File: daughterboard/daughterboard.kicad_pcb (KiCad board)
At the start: 2 copper layers, 49 x 51 mm, 19 parts, among them J1 Conn_02x07_Odd_Even, J2 Conn_01x01, J3 Conn_01x01, J4 Conn_01x01, J5 Conn_01x01, SW1 SW_Push, SW2 Rotary_Encoder_Switch_Alps, SW3 SW_Push, SW4 SW_Push

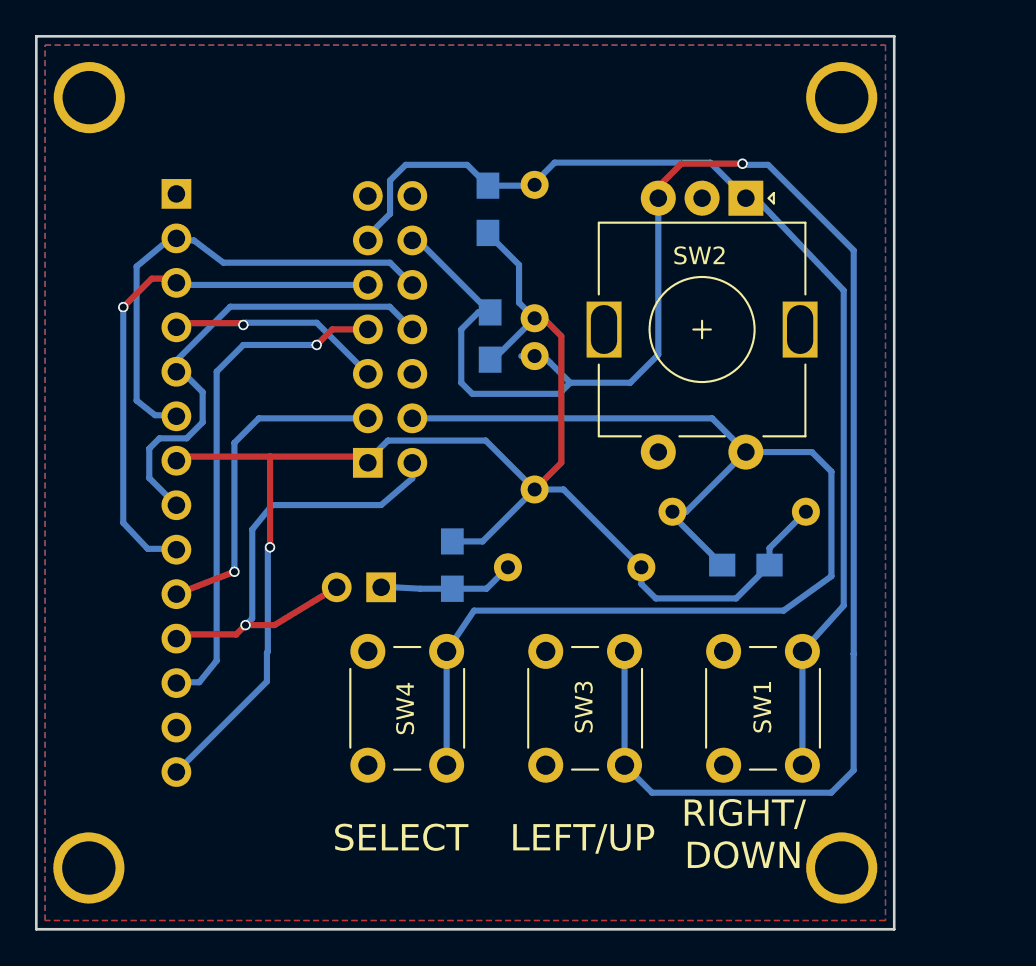
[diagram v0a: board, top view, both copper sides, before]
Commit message: Moved mounting holes to ensure no interference
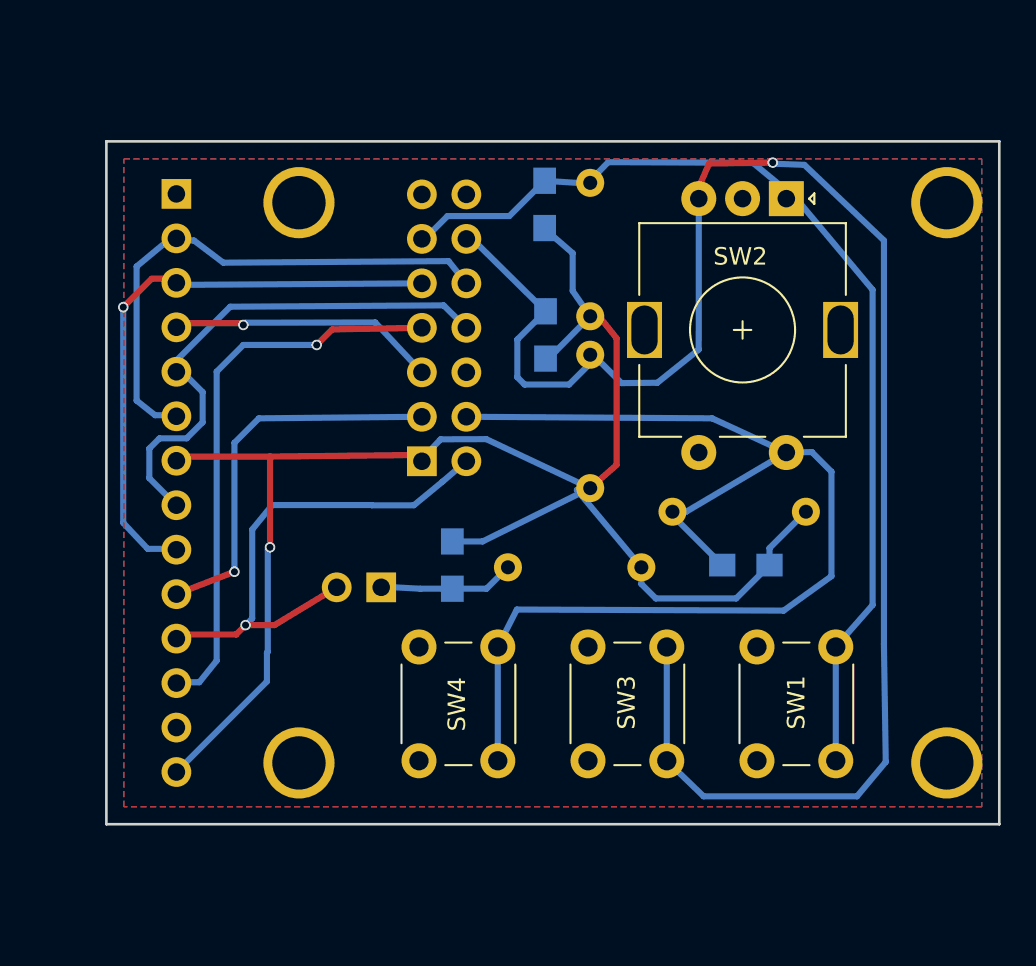
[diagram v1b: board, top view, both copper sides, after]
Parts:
- moved J4 13.4 mm to (111.0, 87.5), turned to 270 degrees
- moved J2 13.4 mm to (111.0, 55.5)
- moved J3 8.49 mm to (148.0, 87.5)
- moved J5 8.49 mm to (148.0, 55.5)
- moved R3 3.25 mm to (125.0, 55.6)
- moved R4 3.18 mm to (127.6, 62.0)
- moved R2 3.18 mm to (127.6, 71.8)
- moved R1 3.16 mm to (125.1, 63.1)
- moved J1 3.09 mm to (118.0, 70.3)
- moved SW4 2.93 mm to (117.9, 87.4)
- moved SW3 2.43 mm to (127.5, 87.4)
- moved SW2 2.31 mm to (138.8, 55.3)
- moved SW1 1.92 mm to (137.2, 87.4)
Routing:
- net CS5: track 71.4 -> 66.9 mm
- net +5V: track 91.9 -> 96.1 mm
- net MISO: track 27.4 -> 30.6 mm
- net CS2: track 12.8 -> 16.0 mm
- net CS1: track 29.4 -> 32.5 mm
- net CS3: track 19.8 -> 22.8 mm
- net MOSI: track 30.5 -> 33.5 mm
- net SCK: track 27.4 -> 30.5 mm
- net INTF2: track 102.0 -> 98.9 mm
- net CS4: track 27.3 -> 29.8 mm
- net INTF1: track 62.5 -> 60.6 mm
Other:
- board size 49 x 51 mm -> 51 x 39 mm
- board text added: "VNA LCD INTERFACE KW4TI CC-BY-SA 4.0"
- board text removed: "LEFT/UP"
- board text removed: "RIGHT/ DOWN"
- board text removed: "SELECT"
- board text removed: "VNA LCD INTERFACE BOARD ILI9341/ILI9488 SPI LCD TOUCHSCREEN BY KW4TI CC-BY-SA 4.0"

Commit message: Added debouncing capacitors
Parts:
- added C1: C_Small, Capacitors_SMD:C_0805_HandSoldering, B.Cu at (145.5, 69.0)
- added C2: C_Small, Capacitors_THT:C_Disc_D5.0mm_W2.5mm_P2.50mm, B.Cu at (145.5, 61.9)
- added C3: C_Small, Capacitors_SMD:C_0805_HandSoldering, B.Cu at (145.5, 73.9)
- added C4: C_Small, Capacitors_THT:C_Disc_D5.0mm_W2.5mm_P2.50mm, B.Cu at (148.1, 64.8)
- added C5: C_Small, Capacitors_SMD:C_0805_HandSoldering, B.Cu at (113.9, 81.3)
- added C6: C_Small, Capacitors_THT:C_Disc_D5.0mm_W2.5mm_P2.50mm, B.Cu at (115.6, 78.4)
- moved JP1 2.29 mm to (115.6, 75.2)
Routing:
- net CS5: track 66.9 -> 77.8 mm
- net INTF2: track 98.9 -> 109.2 mm
- net GND: track 0.00 -> 3.32 mm, vias 0 -> 2
- net INTF1: track 60.6 -> 62.5 mm
- net CS4: track 29.8 -> 31.6 mm
- net Net-(JP1-Pad1): track 7.75 -> 8.65 mm

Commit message: Added resistors in discharge debounce
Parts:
- added R10: 100R, Resistors_THT:R_Axial_DIN0207_L6.3mm_D2.5mm_P7.62mm_Horizontal, B.Cu at (145.7, 61.9)
- added R11: 100R, Resistors_SMD:R_0805_HandSoldering, B.Cu at (146.8, 82.5)
- added R12: 100R, Resistors_THT:R_Axial_DIN0207_L6.3mm_D2.5mm_P7.62mm_Horizontal, B.Cu at (148.2, 80.5)
- added R13: 100R, Resistors_SMD:R_0805_HandSoldering, B.Cu at (110.9, 80.3)
- added R14: 100R, Resistors_THT:R_Axial_DIN0207_L6.3mm_D2.5mm_P7.62mm_Horizontal, B.Cu at (115.1, 74.5)
- added R9: 100R, Resistors_SMD:R_0805_HandSoldering, B.Cu at (146.7, 59.7)
- C1, C2, C3, C4, C5, C6: value C_Small -> 100 nF
- R1, R2, R3, R4, R5, R6, R7, R8: value 10k -> 100k
- moved C4 15.1 mm to (145.0, 79.6), turned to 90 degrees
- moved C6 5.76 mm to (111.9, 82.8)
- moved C5 5.08 mm to (115.4, 86.1), turned to 270 degrees
- moved JP1 4.36 mm to (111.6, 77.1), turned to 0 degrees
- moved C1 3.15 mm to (148.7, 69.2), turned to 90 degrees
- moved C2 2.86 mm to (148.4, 62.4), turned to 270 degrees
- moved C3 0.89 mm to (145.4, 73.0), turned to 270 degrees
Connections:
- C1 pad 1: INTF1 -> Net-(C1-Pad1)
- C2 pad 1: INTF1 -> Net-(C1-Pad1)
- C3 pad 1: INTF2 -> Net-(C3-Pad1)
- C4 pad 1: INTF2 -> Net-(C3-Pad1)
- C5 pad 1: CS5 -> Net-(C5-Pad1)
- C6 pad 1: CS5 -> Net-(C5-Pad1)
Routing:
- net Net-(C1-Pad1): track 0.00 -> 15.7 mm
- net Net-(C3-Pad1): track 0.00 -> 15.3 mm
- net Net-(JP1-Pad1): track 8.65 -> 18.4 mm
- net Net-(C5-Pad1): track 0.00 -> 9.42 mm
- net CS5: track 77.8 -> 85.4 mm
- net INTF2: track 109.2 -> 116.6 mm
- net CS4: track 31.6 -> 27.5 mm
- net GND: track 3.32 -> 6.33 mm, vias 2 -> 0
- net +5V: track 96.1 -> 99.0 mm
- net INTF1: track 62.5 -> 64.4 mm
- net CS3: track 22.8 -> 21.9 mm

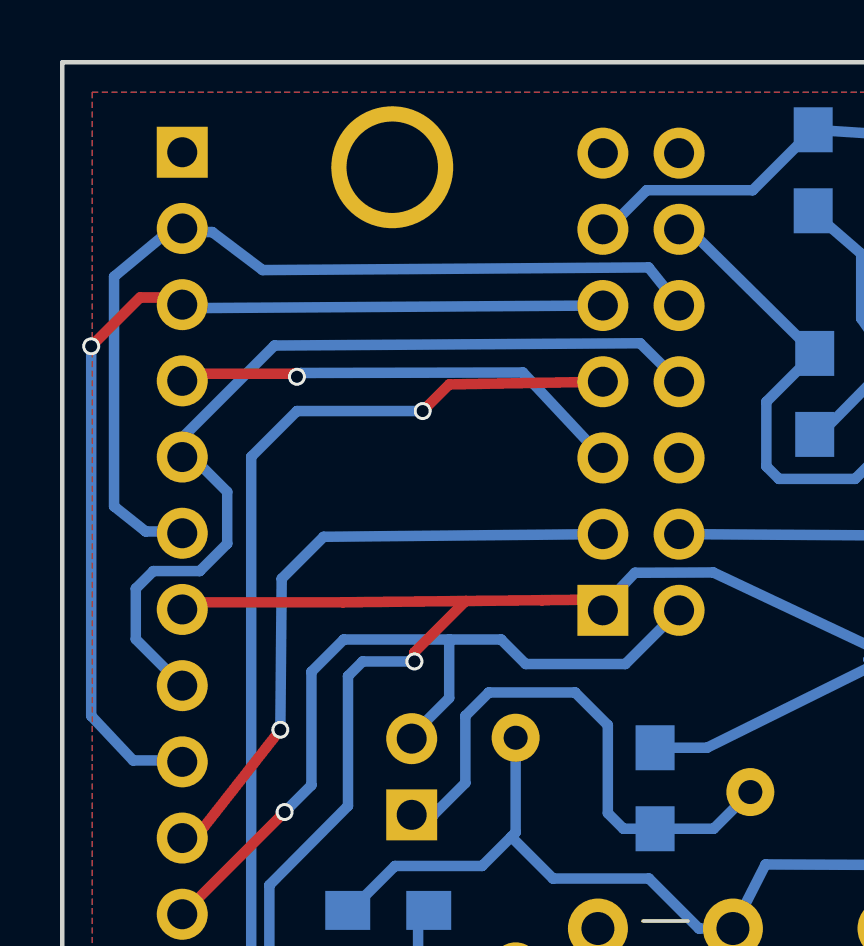
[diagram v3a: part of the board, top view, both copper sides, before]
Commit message: Added vacuum holes to fixture
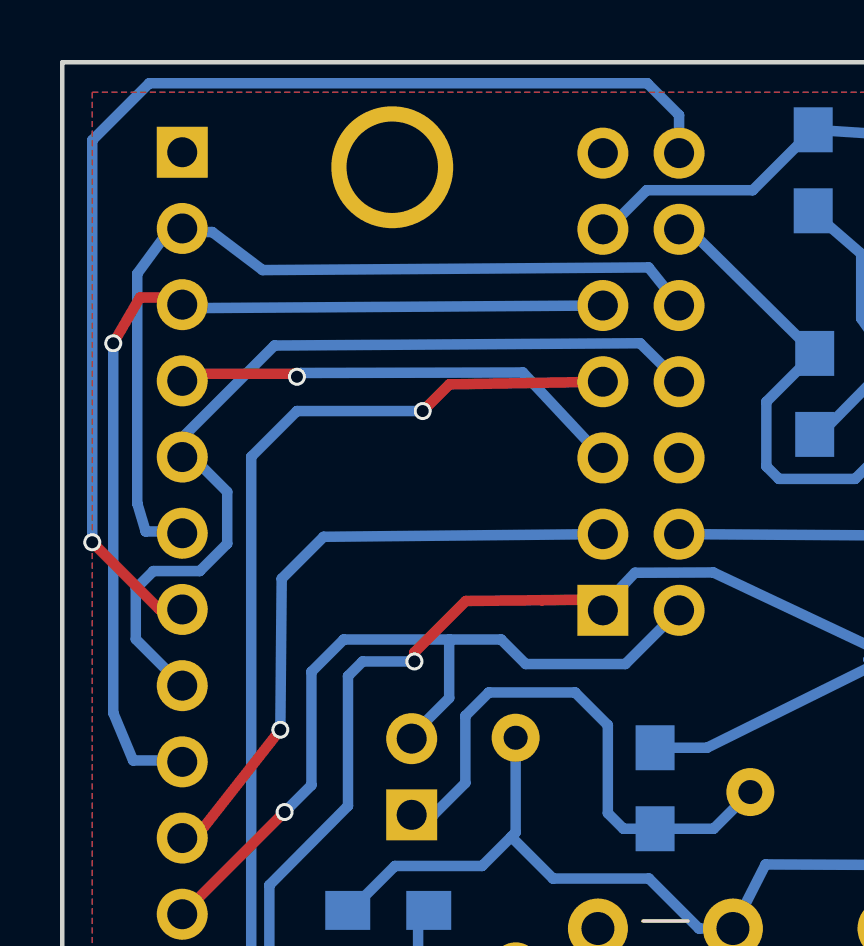
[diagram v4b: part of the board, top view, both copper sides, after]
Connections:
- DISP1 pad 7: +5V -> LEDPWR
- J1 pad 14: (no net) -> LEDPWR
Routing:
- net LEDPWR: track 0.00 -> 39.9 mm, vias 0 -> 1
- net +5V: track 99.0 -> 88.7 mm
- net MISO: track 30.6 -> 29.6 mm
- net MOSI: track 33.5 -> 32.7 mm
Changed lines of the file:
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@@
     (links 68)
     (no_connects 0)
-    (area 99.924999 51.924999 151.075001 91.075001)
+    (area 99.924999 51.525 164.1584 92.247619)
     (thickness 1.6)
     (drawings 6)
-    (tracks 246)
+    (tracks 252)
     (zones 0)
     (modules 31)
-    (nets 17)
+    (nets 18)
   )
   (page A4)
@@
   (net 15 "Net-(C3-Pad1)")
   (net 16 "Net-(C5-Pad1)")
+  (net 17 LEDPWR)
   (net_class Default "This is the default net class."
     (clearance 0.2)
@@
     (add_net INTF1)
     (add_net INTF2)
+    (add_net LEDPWR)
     (add_net MISO)
     (add_net MOSI)
@@
       (net 12 INTF2))
     (pad 13 thru_hole oval (at 0 -15.24) (size 1.7 1.7) (drill 1) (layers *.Cu *.Mask))
-    (pad 14 thru_hole oval (at 2.54 -15.24) (size 1.7 1.7) (drill 1) (layers *.Cu *.Mask))
+    (pad 14 thru_hole oval (at 2.54 -15.24) (size 1.7 1.7) (drill 1) (layers *.Cu *.Mask)
+      (net 17 LEDPWR))
     (model ${KISYS3DMOD}/Pin_Headers.3dshapes/Pin_Header_Straight_2x07_Pitch2.54mm.wrl
       (at (xyz 0 0 0))
@@
       (net 10 MISO))
     (pad 7 thru_hole oval (at 0 -15.24 180) (size 1.7 1.7) (drill 1) (layers *.Cu *.Mask)
-      (net 1 +5V))
+      (net 17 LEDPWR))
     (pad 8 thru_hole oval (at 0 -17.78 180) (size 1.7 1.7) (drill 1) (layers *.Cu *.Mask)
       (net 8 SCK))
@@
     (effects (font (size 1.5 1.5) (thickness 0.3)) (justify mirror))
   )
-  (segment (start 111.73968 71.97344) (end 111.73968 71.66864) (width 0.35) (layer F.Cu) (net 1))
-  (segment (start 111.73968 71.66864) (end 113.449766 69.958554) (width 0.35) (layer F.Cu) (net 1))
   (segment (start 104.3088 88.02) (end 106.90352 85.4456) (width 0.35) (layer B.Cu) (net 1))
   (segment (start 115.976455 69.931225) (end 116.006946 69.931225) (width 0.35) (layer F.Cu) (net 1))
-  (via (at 111.73968 71.97344) (size 0.6) (drill 0.4) (layers F.Cu B.Cu) (net 1))
-  (segment (start 110.01248 71.97344) (end 111.73968 71.97344) (width 0.35) (layer B.Cu) (net 1))
-  (segment (start 109.5248 72.46112) (end 110.01248 71.97344) (width 0.35) (layer B.Cu) (net 1))
   (segment (start 109.5248 76.78928) (end 109.5248 72.46112) (width 0.35) (layer B.Cu) (net 1))
   (segment (start 106.90352 79.43088) (end 109.5248 76.78928) (width 0.35) (layer B.Cu) (net 1))
@@
   (segment (start 119.761 74.85) (end 121.492 74.85) (width 0.35) (layer B.Cu) (net 1))
   (segment (start 121.492 74.85) (end 127.635 71.8058) (width 0.35) (layer B.Cu) (net 1) (status 20))
-  (segment (start 103.57104 70.0024) (end 109.347 70.0024) (width 0.35) (layer F.Cu) (net 1))
-  (segment (start 109.347 70.0024) (end 113.449766 69.958554) (width 0.35) (layer F.Cu) (net 1) (status 20))
   (segment (start 113.449766 69.958554) (end 116.006946 69.931225) (width 0.35) (layer F.Cu) (net 1) (status 20))
   (segment (start 116.006946 69.931225) (end 117.6655 69.9135) (width 0.35) (layer F.Cu) (net 1) (status 20))
   (segment (start 117.6655 69.9135) (end 118.0211 70.2691) (width 0.35) (layer F.Cu) (net 1) (status 30))
-  (segment (start 103.92664 70.358) (end 103.57104 70.0024) (width 0.35) (layer B.Cu) (net 1))
+  (segment (start 111.73968 71.97344) (end 111.73968 71.66864) (width 0.35) (layer F.Cu) (net 1))
+  (segment (start 111.73968 71.66864) (end 113.449766 69.958554) (width 0.35) (layer F.Cu) (net 1))
+  (via (at 111.73968 71.97344) (size 0.6) (drill 0.4) (layers F.Cu B.Cu) (net 1))
+  (segment (start 110.01248 71.97344) (end 111.73968 71.97344) (width 0.35) (layer B.Cu) (net 1))
+  (segment (start 109.5248 72.46112) (end 110.01248 71.97344) (width 0.35) (layer B.Cu) (net 1))
   (segment (start 111.64824 74.54646) (end 111.64824 74.44232) (width 0.35) (layer B.Cu) (net 2))
   (segment (start 111.64824 74.44232) (end 112.89792 73.19264) (width 0.35) (layer B.Cu) (net 2))
@@
   (segment (start 103.57104 59.8424) (end 102.5906 59.8424) (width 0.35) (layer F.Cu) (net 9))
   (segment (start 102.362 75.2729) (end 103.67264 75.2729) (width 0.35) (layer B.Cu) (net 9))
-  (segment (start 100.965 73.787) (end 102.362 75.2729) (width 0.35) (layer B.Cu) (net 9))
-  (segment (start 100.965 61.468) (end 100.965 73.787) (width 0.35) (layer B.Cu) (net 9))
-  (via (at 100.965 61.468) (size 0.6) (drill 0.4) (layers F.Cu B.Cu) (net 9))
-  (segment (start 102.5906 59.8424) (end 100.965 61.468) (width 0.35) (layer F.Cu) (net 9))
+  (segment (start 101.7 73.687) (end 102.362 75.2729) (width 0.35) (layer B.Cu) (net 9))
+  (segment (start 101.7 61.368) (end 101.7 73.687) (width 0.35) (layer B.Cu) (net 9))
+  (via (at 101.7 61.368) (size 0.6) (drill 0.4) (layers F.Cu B.Cu) (net 9))
+  (segment (start 102.5906 59.8424) (end 101.7 61.368) (width 0.35) (layer F.Cu) (net 9))
   (segment (start 118.0211 60.1091) (end 103.92664 60.198) (width 0.35) (layer B.Cu) (net 9) (status 10))
   (segment (start 103.92664 60.198) (end 103.57104 59.8424) (width 0.35) (layer B.Cu) (net 9))
   (segment (start 103.96474 67.6402) (end 102.7811 67.6402) (width 0.35) (layer B.Cu) (net 10))
-  (segment (start 101.727 59.14644) (end 103.518021 57.660232) (width 0.35) (layer B.Cu) (net 10))
-  (segment (start 101.727 66.802) (end 101.727 59.14644) (width 0.35) (layer B.Cu) (net 10))
-  (segment (start 102.7811 67.6402) (end 101.727 66.802) (width 0.35) (layer B.Cu) (net 10))
+  (segment (start 102.5 59.04644) (end 103.518021 57.660232) (width 0.35) (layer B.Cu) (net 10))
+  (segment (start 102.5 66.702) (end 102.5 59.04644) (width 0.35) (layer B.Cu) (net 10))
+  (segment (start 102.7811 67.6402) (end 102.5 66.702) (width 0.35) (layer B.Cu) (net 10))
   (segment (start 103.518021 57.660232) (end 105.001381 57.660232) (width 0.35) (layer B.Cu) (net 10))
   (segment (start 119.5451 58.8391) (end 120.5611 60.1091) (width 0.35) (layer B.Cu) (net 10) (status 20))
@@
   (segment (start 111.8616 80.62594) (end 112.21592 80.27162) (width 0.35) (layer B.Cu) (net 16))
   (segment (start 111.9686 80.51894) (end 112.21592 80.27162) (width 0.35) (layer B.Cu) (net 16))
+  (segment (start 120.5611 55.0291) (end 120.5611 53.7611) (width 0.35) (layer B.Cu) (net 17))
+  (segment (start 101 68) (end 103.24 70.24) (width 0.35) (layer F.Cu) (net 17))
+  (via (at 101 68) (size 0.6) (drill 0.4) (layers F.Cu B.Cu) (net 17))
+  (segment (start 101 54.6) (end 101 68) (width 0.35) (layer B.Cu) (net 17))
+  (segment (start 102.9 52.7) (end 101 54.6) (width 0.35) (layer B.Cu) (net 17))
+  (segment (start 119.5 52.7) (end 102.9 52.7) (width 0.35) (layer B.Cu) (net 17))
+  (segment (start 120.5611 53.7611) (end 119.5 52.7) (width 0.35) (layer B.Cu) (net 17))
+  (segment (start 103.24 70.24) (end 104 70.24) (width 0.35) (layer F.Cu) (net 17))
+  (segment (start 103.92664 70.358) (end 103.57104 70.0024) (width 0.35) (layer B.Cu) (net 17))
   (zone (net 6) (net_name GND) (layer F.Cu) (hatch edge 0.508)
     (connect_pads (clearance 0.5))
